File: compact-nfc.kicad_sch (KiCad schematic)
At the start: 17 parts, among them U1 ITR9702, U2 PN5321A3HN_C1xx

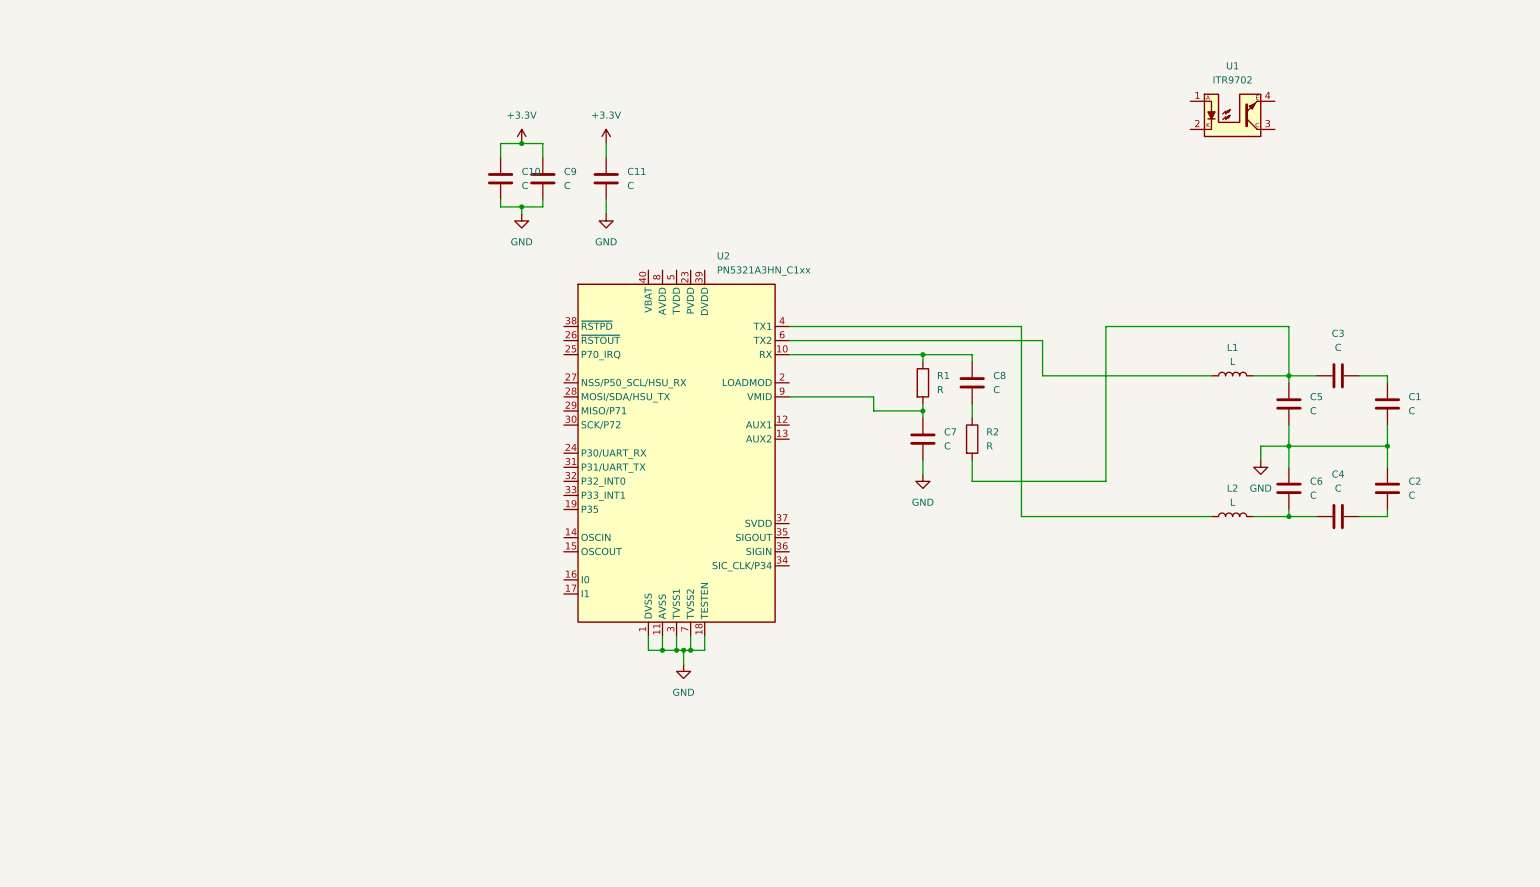
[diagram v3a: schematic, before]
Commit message: Add more components from reference schematic
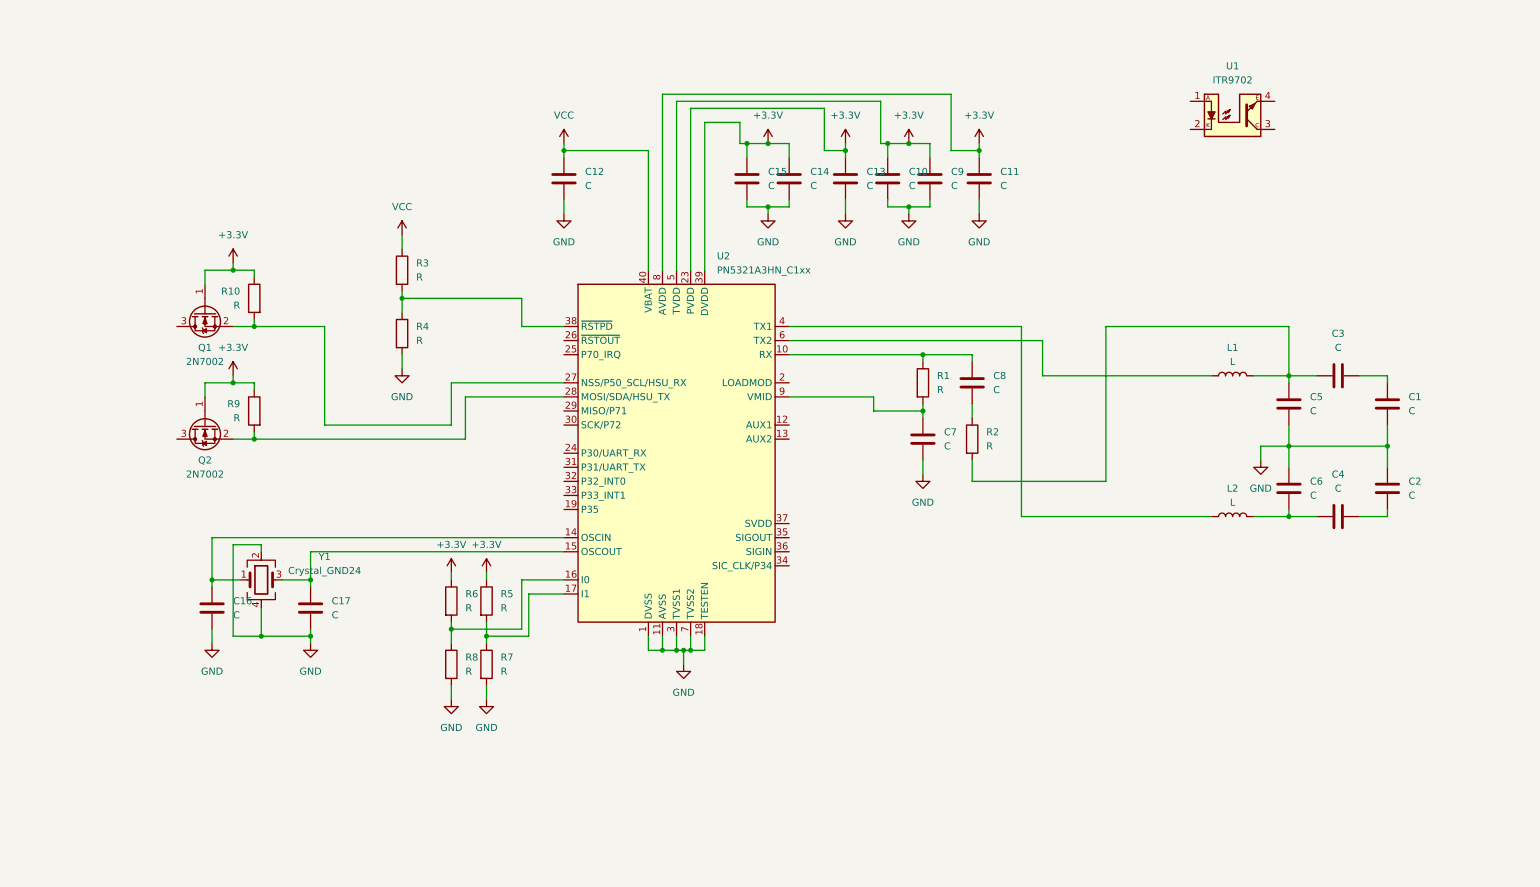
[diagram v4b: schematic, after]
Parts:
- added C12, C13, C14, C15, C16, C17: C, Capacitor_SMD:C_0805_2012Metric_Pad1.18x1.45mm_HandSolder, symbol Device:C
- added Q1, Q2: 2N7002, Package_TO_SOT_SMD:SOT-23, symbol Transistor_FET:2N7002
- added R10, R3, R4, R5, R6, R7, R8, R9: R, Resistor_SMD:R_0805_2012Metric_Pad1.20x1.40mm_HandSolder, symbol Device:R
- added Y1: Crystal_GND24, Crystal:Crystal_SMD_3225-4Pin_3.2x2.5mm_HandSoldering, symbol Device:Crystal_GND24
- C10, C11, C9: footprint (none) -> Capacitor_SMD:C_0805_2012Metric_Pad1.18x1.45mm_HandSolder
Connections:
- net +3.3V: now also U2.23 (PVDD), U2.39 (DVDD), U2.5 (TVDD), U2.8 (AVDD), C13.1, C14.1, C15.1, Q1.1 (G), Q2.1 (G), R10.1, R5.1, R6.1, R9.1
- net GND: now also C12.2, C13.2, C14.2, C15.2, C16.1, C17.1, R4.2, R7.2, R8.2, Y1.2, Y1.4
- net at U2.14 (OSCIN): now also C16.2, Y1.1
- net at U2.15 (OSCOUT): now also C17.2, Y1.3
- net at U2.16 (I0): now also R6.2, R8.1
- net at U2.17 (I1): now also R5.2, R7.1
- net at U2.27 (NSS/P50_SCL/HSU_RX): now also Q1.2 (S), R10.2
- net at U2.28 (MOSI/SDA/HSU_TX): now also Q2.2 (S), R9.2
- net at U2.38 (~{RSTPD}): now also R3.2, R4.1
- net VCC: now reaches U2.40 (VBAT)
- net VCC: now also C12.1, R3.1
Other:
- moved on the sheet: C10, C11, C9

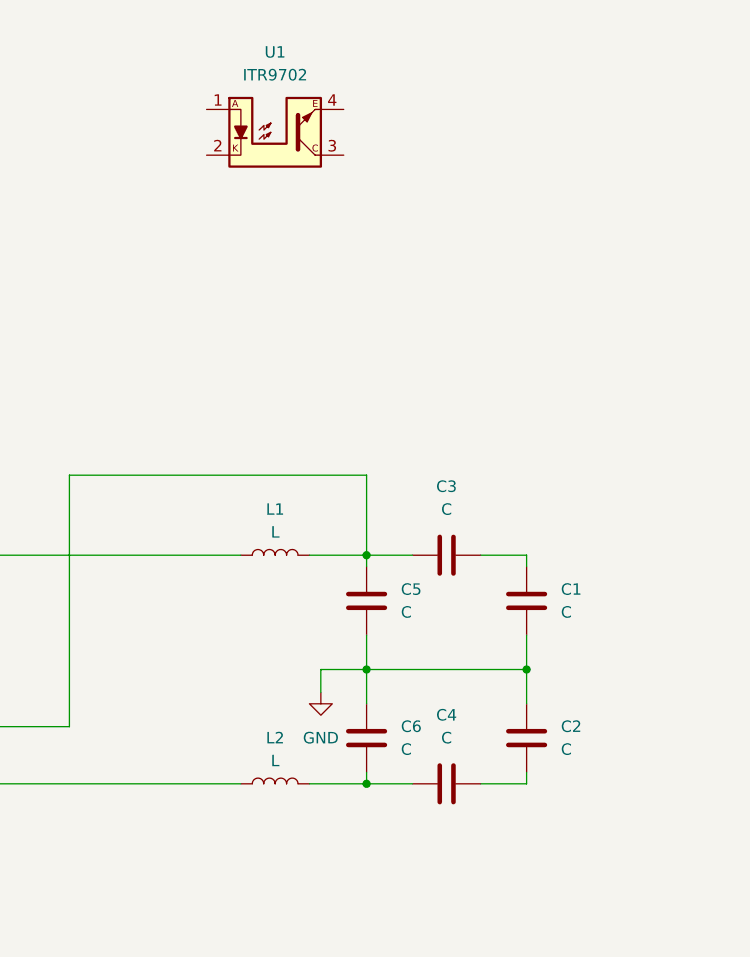
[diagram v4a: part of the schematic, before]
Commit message: Start coil construction on PCB
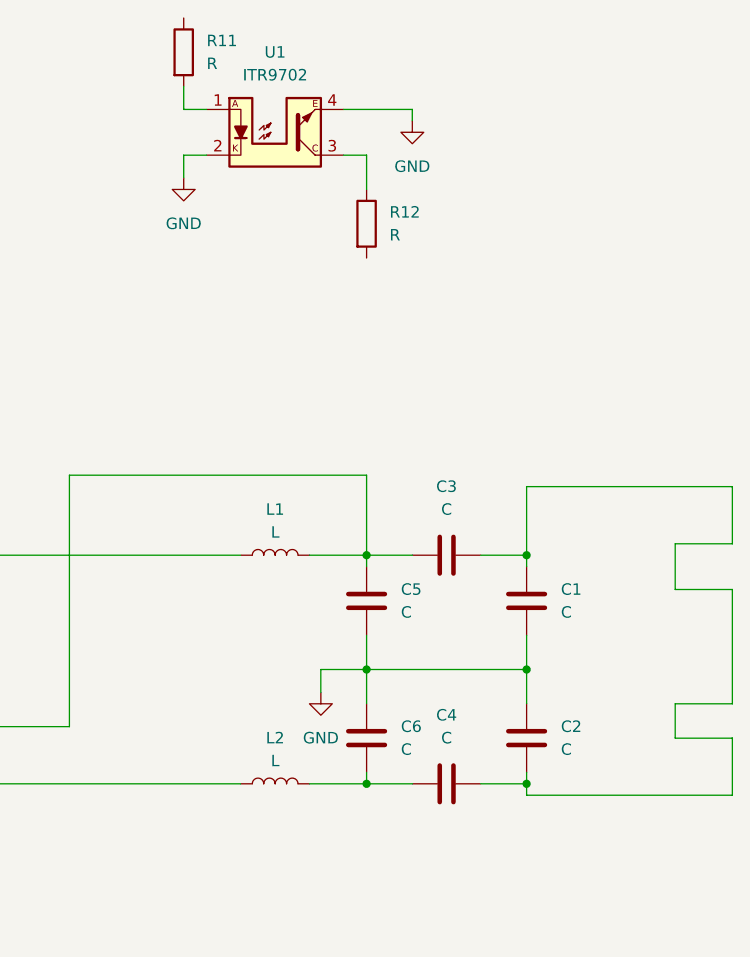
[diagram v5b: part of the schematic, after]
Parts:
- added R11, R12: R, Resistor_SMD:R_0805_2012Metric_Pad1.20x1.40mm_HandSolder, symbol Device:R
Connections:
- net GND: now also U1.2, U1.4
- net at C2.2, C4.2: now also C1.1, C3.2
- net at U1.1: now also R11.2
- net at U1.3: now also R12.1
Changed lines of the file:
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@@
   (junction (at 124.46 138.43) (diameter 0) (color 0 0 0 0)
   )
+  (junction (at 255.27 114.3) (diameter 0) (color 0 0 0 0)
+  )
   (junction (at 50.8 100.33) (diameter 0) (color 0 0 0 0)
   )
@@
   (junction (at 255.27 101.6) (diameter 0) (color 0 0 0 0)
   )
+  (junction (at 255.27 88.9) (diameter 0) (color 0 0 0 0)
+  )
   (junction (at 128.27 138.43) (diameter 0) (color 0 0 0 0)
   )
@@
     (stroke (width 0) (type default))
   )
+  (wire (pts (xy 217.17 44.45) (xy 217.17 46.99))
+    (stroke (width 0) (type default))
+  )
   (wire (pts (xy 180.34 107.95) (xy 204.47 107.95))
     (stroke (width 0) (type default))
@@
     (stroke (width 0) (type default))
   )
+  (wire (pts (xy 271.78 87.63) (xy 271.78 92.71))
+    (stroke (width 0) (type default))
+  )
   (wire (pts (xy 77.47 73.66) (xy 77.47 74.93))
     (stroke (width 0) (type default))
@@
     (stroke (width 0) (type default))
   )
+  (wire (pts (xy 234.95 44.45) (xy 237.49 44.45))
+    (stroke (width 0) (type default))
+  )
+  (wire (pts (xy 278.13 105.41) (xy 271.78 105.41))
+    (stroke (width 0) (type default))
+  )
   (wire (pts (xy 41.91 90.17) (xy 41.91 92.71))
     (stroke (width 0) (type default))
@@
     (stroke (width 0) (type default))
   )
+  (wire (pts (xy 217.17 39.37) (xy 219.71 39.37))
+    (stroke (width 0) (type default))
+  )
   (wire (pts (xy 147.32 80.01) (xy 189.23 80.01))
     (stroke (width 0) (type default))
@@
     (stroke (width 0) (type default))
   )
+  (wire (pts (xy 234.95 39.37) (xy 242.57 39.37))
+    (stroke (width 0) (type default))
+  )
   (wire (pts (xy 46.99 68.58) (xy 46.99 69.85))
     (stroke (width 0) (type default))
@@
     (stroke (width 0) (type default))
   )
+  (wire (pts (xy 278.13 115.57) (xy 255.27 115.57))
+    (stroke (width 0) (type default))
+  )
   (wire (pts (xy 171.45 85.09) (xy 180.34 85.09))
     (stroke (width 0) (type default))
@@
     (stroke (width 0) (type default))
   )
+  (wire (pts (xy 237.49 44.45) (xy 237.49 48.26))
+    (stroke (width 0) (type default))
+  )
   (wire (pts (xy 77.47 63.5) (xy 77.47 66.04))
     (stroke (width 0) (type default))
@@
     (stroke (width 0) (type default))
   )
+  (wire (pts (xy 255.27 81.28) (xy 278.13 81.28))
+    (stroke (width 0) (type default))
+  )
   (wire (pts (xy 180.34 104.14) (xy 180.34 107.95))
     (stroke (width 0) (type default))
@@
     (stroke (width 0) (type default))
   )
+  (wire (pts (xy 219.71 44.45) (xy 217.17 44.45))
+    (stroke (width 0) (type default))
+  )
   (wire (pts (xy 204.47 80.01) (xy 237.49 80.01))
     (stroke (width 0) (type default))
@@
     (stroke (width 0) (type default))
   )
+  (wire (pts (xy 278.13 92.71) (xy 278.13 105.41))
+    (stroke (width 0) (type default))
+  )
   (wire (pts (xy 162.56 92.71) (xy 162.56 95.25))
     (stroke (width 0) (type default))
@@
     (stroke (width 0) (type default))
   )
+  (wire (pts (xy 271.78 105.41) (xy 271.78 109.22))
+    (stroke (width 0) (type default))
+  )
   (wire (pts (xy 99.06 125.73) (xy 106.68 125.73))
     (stroke (width 0) (type default))
@@
     (stroke (width 0) (type default))
   )
+  (wire (pts (xy 217.17 36.83) (xy 217.17 39.37))
+    (stroke (width 0) (type default))
+  )
+  (wire (pts (xy 271.78 92.71) (xy 278.13 92.71))
+    (stroke (width 0) (type default))
+  )
+  (wire (pts (xy 255.27 115.57) (xy 255.27 114.3))
+    (stroke (width 0) (type default))
+  )
   (wire (pts (xy 86.36 90.17) (xy 86.36 97.79))
     (stroke (width 0) (type default))
@@
     (stroke (width 0) (type default))
   )
+  (wire (pts (xy 271.78 109.22) (xy 278.13 109.22))
+    (stroke (width 0) (type default))
+  )
   (wire (pts (xy 172.72 46.99) (xy 168.91 46.99))
     (stroke (width 0) (type default))
@@
     (stroke (width 0) (type default))
   )
+  (wire (pts (xy 278.13 81.28) (xy 278.13 87.63))
+    (stroke (width 0) (type default))
+  )
   (wire (pts (xy 157.48 57.15) (xy 157.48 59.69))
     (stroke (width 0) (type default))
   )
+  (wire (pts (xy 242.57 39.37) (xy 242.57 40.64))
+    (stroke (width 0) (type default))
+  )
   (wire (pts (xy 50.8 99.06) (xy 50.8 100.33))
     (stroke (width 0) (type default))
@@
     (stroke (width 0) (type default))
   )
+  (wire (pts (xy 278.13 87.63) (xy 271.78 87.63))
+    (stroke (width 0) (type default))
+  )
   (wire (pts (xy 147.32 82.55) (xy 193.04 82.55))
     (stroke (width 0) (type default))
@@
     (stroke (width 0) (type default))
   )
+  (wire (pts (xy 278.13 109.22) (xy 278.13 115.57))
+    (stroke (width 0) (type default))
+  )
   (wire (pts (xy 139.7 49.53) (xy 139.7 46.99))
     (stroke (width 0) (type default))
@@
   )
   (wire (pts (xy 124.46 135.89) (xy 124.46 138.43))
+    (stroke (width 0) (type default))
+  )
+  (wire (pts (xy 255.27 88.9) (xy 255.27 81.28))
     (stroke (width 0) (type default))
   )
@@
     )
   )
+  (symbol (lib_id "Device:R") (at 237.49 52.07 0) (unit 1)
+    (in_bom yes) (on_board yes) (dnp no) (fields_autoplaced)
+    (property "Reference" "R12" (at 240.03 50.8 0)
+      (effects (font (size 1.27 1.27)) (justify left))
+    )
+    (property "Value" "R" (at 240.03 53.34 0)
+      (effects (font (size 1.27 1.27)) (justify left))
+    )
+    (property "Footprint" "Resistor_SMD:R_0805_2012Metric_Pad1.20x1.40mm_HandSolder" (at 235.712 52.07 90)
+      (effects (font (size 1.27 1.27)) hide)
+    )
+    (property "Datasheet" "~" (at 237.49 52.07 0)
+      (effects (font (size 1.27 1.27)) hide)
+    )
+    (pin "2")
+    (pin "1")
+    (instances
+      (project "compact-nfc"
+        (path "/21d4213f-f9dc-4f6d-96b5-1a03aba56c6c"
+          (reference "R12") (unit 1)
+        )
+      )
+    )
+  )
   (symbol (lib_id "Device:C") (at 157.48 53.34 0) (unit 1)
     (in_bom yes) (on_board yes) (dnp no) (fields_autoplaced)
@@
     )
   )
+  (symbol (lib_id "power:GND") (at 242.57 40.64 0) (unit 1)
+    (in_bom yes) (on_board yes) (dnp no) (fields_autoplaced)
+    (property "Reference" "#PWR025" (at 242.57 46.99 0)
+      (effects (font (size 1.27 1.27)) hide)
+    )
+    (property "Value" "GND" (at 242.57 45.72 0)
+      (effects (font (size 1.27 1.27)))
+    )
+    (property "Footprint" "" (at 242.57 40.64 0)
+      (effects (font (size 1.27 1.27)) hide)
+    )
+    (property "Datasheet" "" (at 242.57 40.64 0)
+      (effects (font (size 1.27 1.27)) hide)
+    )
+    (pin "1")
+    (instances
+      (project "compact-nfc"
+        (path "/21d4213f-f9dc-4f6d-96b5-1a03aba56c6c"
+          (reference "#PWR025") (unit 1)
+        )
+      )
+    )
+  )
   (symbol (lib_id "Device:C") (at 180.34 90.17 180) (unit 1)
     (in_bom yes) (on_board yes) (dnp no) (fields_autoplaced)
@@
         )
       )
+    )
+  )
+  (symbol (lib_id "Device:R") (at 217.17 33.02 0) (unit 1)
+    (in_bom yes) (on_board yes) (dnp no) (fields_autoplaced)
+    (property "Reference" "R11" (at 219.71 31.75 0)
+      (effects (font (size 1.27 1.27)) (justify left))
+    )
+    (property "Value" "R" (at 219.71 34.29 0)
+      (effects (font (size 1.27 1.27)) (justify left))
+    )
+    (property "Footprint" "Resistor_SMD:R_0805_2012Metric_Pad1.20x1.40mm_HandSolder" (at 215.392 33.02 90)
+      (effects (font (size 1.27 1.27)) hide)
+    )
+    (property "Datasheet" "~" (at 217.17 33.02 0)
+      (effects (font (size 1.27 1.27)) hide)
+    )
+    (pin "2")
+    (pin "1")
+    (instances
+      (project "compact-nfc"
+        (path "/21d4213f-f9dc-4f6d-96b5-1a03aba56c6c"
+          (reference "R11") (unit 1)
+        )
+      )
+    )
+  )
+  (symbol (lib_id "power:GND") (at 217.17 46.99 0) (unit 1)
+    (in_bom yes) (on_board yes) (dnp no) (fields_autoplaced)
+    (property "Reference" "#PWR024" (at 217.17 53.34 0)
+      (effects (font (size 1.27 1.27)) hide)
+    )
+    (property "Value" "GND" (at 217.17 52.07 0)
+      (effects (font (size 1.27 1.27)))
+    )
+    (property "Footprint" "" (at 217.17 46.99 0)
+      (effects (font (size 1.27 1.27)) hide)
+    )
+    (property "Datasheet" "" (at 217.17 46.99 0)
+      (effects (font (size 1.27 1.27)) hide)
+    )
+    (pin "1")
+    (instances
+      (project "compact-nfc"
+        (path "/21d4213f-f9dc-4f6d-96b5-1a03aba56c6c"
+          (reference "#PWR024") (unit 1)
+        )
+      )

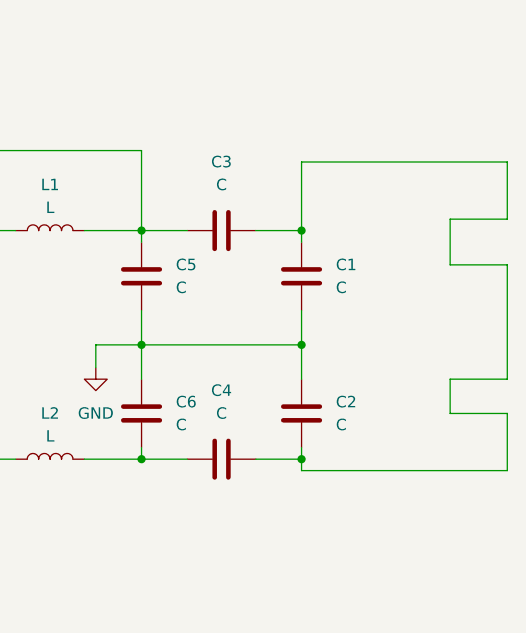
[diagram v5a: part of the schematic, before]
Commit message: Add coil as PCB library component
- Add L_NFC_PCB footprint (Inductor_PCB.pretty)
- Add coil_pcb symbol
- Update fp-lib-table and sym-lib-table
- Update PCB and schematic with coil placement
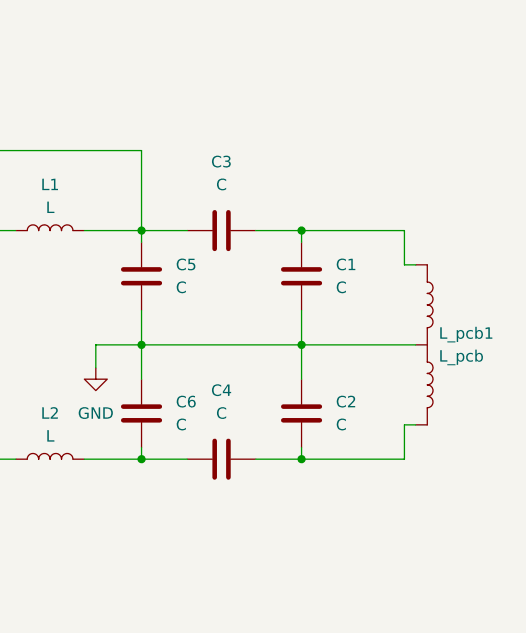
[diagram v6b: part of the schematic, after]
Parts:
- added L_pcb1: L_pcb, Inductor_PCB:L_NFC_PCB, symbol coil_pcb:L_pcb
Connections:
- net GND: now also L_pcb1.2
- net at C2.2, C4.2: now also L_pcb1.3; no longer C1.1, C3.2
- new net: C1.1, C3.2, L_pcb1.1
